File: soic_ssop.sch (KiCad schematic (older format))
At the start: 2 parts, among them P8 CONN_8, P9 CONN_8

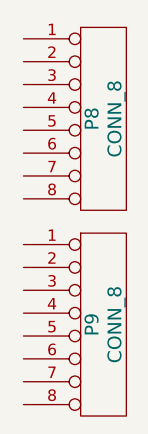
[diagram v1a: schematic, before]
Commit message: most erc errors fixed
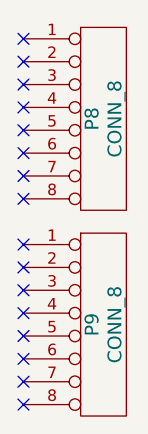
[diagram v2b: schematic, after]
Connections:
- no-connect marks 0 -> 16
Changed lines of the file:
@@
-EESchema Schematic File Version 2  date 03-08-2013 18:53:09
+EESchema Schematic File Version 2
 LIBS:power
 LIBS:device
@@
 	1    0    0    -1
 $EndComp
+NoConn ~ 3050 2250
+NoConn ~ 3050 2350
+NoConn ~ 3050 2450
+NoConn ~ 3050 2550
+NoConn ~ 3050 2650
+NoConn ~ 3050 2750
+NoConn ~ 3050 2850
+NoConn ~ 3050 2950
+NoConn ~ 3050 3150
+NoConn ~ 3050 3250
+NoConn ~ 3050 3350
+NoConn ~ 3050 3450
+NoConn ~ 3050 3550
+NoConn ~ 3050 3650
+NoConn ~ 3050 3750
+NoConn ~ 3050 3850
 $EndSCHEMATC

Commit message: ftdi done + breakout done
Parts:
- added ??1, U4: 74LVC138AD, ~, symbol 74LVC138AD
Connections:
- net at P8.1 (P1): now also ??1.8 (GND), U4.1 (A0)
- net at P8.2 (P2): now also ??1.7 (/Y7), U4.2 (A1)
- net at P8.3 (P3): now also ??1.6 (E3), U4.3 (A2)
- net at P8.4 (P4): now also ??1.5 (/E2), U4.4 (/E1)
- net at P8.5 (P5): now also ??1.4 (/E1), U4.5 (/E2)
- net at P8.6 (P6): now also ??1.3 (A2), U4.6 (E3)
- net at P8.7 (P7): now also ??1.2 (A1), U4.7 (/Y7)
- net at P8.8 (P8): now also ??1.1 (A0), U4.8 (GND)
- net at P9.1 (P1): now also ??1.9 (/Y6), U4.16 (VCC)
- net at P9.2 (P2): now also ??1.10 (/Y5), U4.15 (/Y0)
- net at P9.3 (P3): now also ??1.11 (/Y4), U4.14 (/Y1)
- net at P9.4 (P4): now also ??1.12 (/Y3), U4.13 (/Y2)
- net at P9.5 (P5): now also ??1.13 (/Y2), U4.12 (/Y3)
- net at P9.6 (P6): now also ??1.14 (/Y1), U4.11 (/Y4)
- net at P9.7 (P7): now also ??1.15 (/Y0), U4.10 (/Y5)
- net at P9.8 (P8): now also ??1.16 (VCC), U4.9 (/Y6)
- no-connect marks 16 -> 0
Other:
- moved on the sheet: P8, P9
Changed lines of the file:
@@
-EESchema Schematic File Version 2
+EESchema Schematic File Version 2  date 03-08-2013 21:17:06
 LIBS:power
 LIBS:device
@@
 L CONN_8 P8
 U 1 1 51FCB26D
-P 3400 2600
-F 0 "P8" V 3350 2600 60  0000 C CNN
-F 1 "CONN_8" V 3450 2600 60  0000 C CNN
-F 2 "" H 3400 2600 60  0000 C CNN
-F 3 "" H 3400 2600 60  0000 C CNN
-	1    3400 2600
-	1    0    0    -1
+P 3250 2600
+F 0 "P8" V 3200 2600 60  0000 C CNN
+F 1 "CONN_8" V 3300 2600 60  0000 C CNN
+F 2 "" H 3250 2600 60  0000 C CNN
+F 3 "" H 3250 2600 60  0000 C CNN
+	1    3250 2600
+	-1   0    0    -1
 $EndComp
 $Comp
 L CONN_8 P9
 U 1 1 51FCB27C
-P 3400 3500
-F 0 "P9" V 3350 3500 60  0000 C CNN
-F 1 "CONN_8" V 3450 3500 60  0000 C CNN
-F 2 "" H 3400 3500 60  0000 C CNN
-F 3 "" H 3400 3500 60  0000 C CNN
-	1    3400 3500
+P 4950 2600
+F 0 "P9" V 4900 2600 60  0000 C CNN
+F 1 "CONN_8" V 5000 2600 60  0000 C CNN
+F 2 "" H 4950 2600 60  0000 C CNN
+F 3 "" H 4950 2600 60  0000 C CNN
+	1    4950 2600
 	1    0    0    -1
 $EndComp
-NoConn ~ 3050 2250
-NoConn ~ 3050 2350
-NoConn ~ 3050 2450
-NoConn ~ 3050 2550
-NoConn ~ 3050 2650
-NoConn ~ 3050 2750
-NoConn ~ 3050 2850
-NoConn ~ 3050 2950
-NoConn ~ 3050 3150
-NoConn ~ 3050 3250
-NoConn ~ 3050 3350
-NoConn ~ 3050 3450
-NoConn ~ 3050 3550
-NoConn ~ 3050 3650
-NoConn ~ 3050 3750
-NoConn ~ 3050 3850
+$Comp
+L 74LVC138AD ??1
+U 1 1 51FD6D10
+P 4100 2650
+F 0 "??1" H 4100 2650 60  0000 C CNN
+F 1 "74LVC138AD" H 4100 2650 60  0000 C CNN
+F 2 "~" H 4100 2650 60  0000 C CNN
+F 3 "~" H 4100 2650 60  0000 C CNN
+	1    4100 2650
+	1    0    0    1
+$EndComp
+$Comp
+L 74LVC138AD U4
+U 1 1 51FD6D1D
+P 4100 2550
+F 0 "U4" H 4100 2550 60  0000 C CNN
+F 1 "74LVC138AD" H 4100 2550 60  0000 C CNN
+F 2 "~" H 4100 2550 60  0000 C CNN
+F 3 "~" H 4100 2550 60  0000 C CNN
+	1    4100 2550
+	1    0    0    -1
+$EndComp
 $EndSCHEMATC
